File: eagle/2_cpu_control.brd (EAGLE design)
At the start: 160 x 100 mm, 50 parts, among them IC1 74154N, IC2 74LS139N, IC3 74LS138N, IC4 74LS139N, IC5 74LS00N, IC6 74LS32N, IC8 74LS08N

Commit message: All boards prepared for MMU extension
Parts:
- JP10: device pinhead:2X16 -> pinhead:2X18
- moved JP10 2.54 mm to (105.4, 6.99)
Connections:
- new net /FP: JP10.34
- new net /IO: JP10.35
- new net /NP_FAULT: JP10.36
- new net /WR_FAULT: JP10.33
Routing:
- net ALUOP1: track 84.2 -> 88.9 mm
- net ALUOP0: track 76.4 -> 80.0 mm
- net /LOAD_IR: track 106.6 -> 109.0 mm
- net /MEM2ALULO: track 146.8 -> 149.2 mm
- net /ALULO2MEM: track 143.8 -> 146.0 mm
- net /MEM2ALUHI: track 140.2 -> 141.8 mm
- net BUSCLKA: track 55.5 -> 53.9 mm, vias 2 -> 1
- net /ALUHI2MEM: track 141.2 -> 142.3 mm
- net +5V: track 479.5 -> 480.0 mm

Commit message: Removal of PPC started
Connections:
- removed net /LDPPC: JP10.11
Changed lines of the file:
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@@
 <contactref element="JP10" pad="30"/>
-</signal>
-<signal name="/LDPPC">
-<contactref element="JP10" pad="11"/>
 </signal>
 <signal name="BUSCLKA">

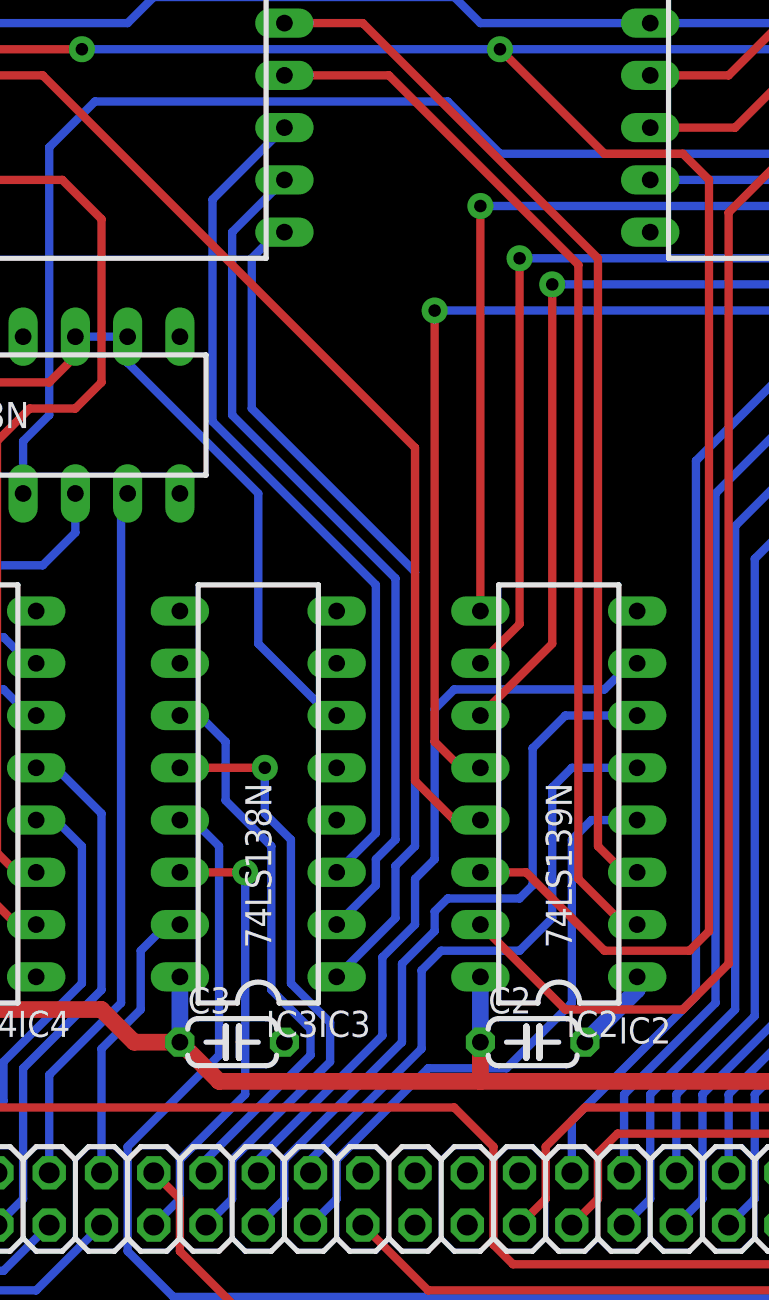
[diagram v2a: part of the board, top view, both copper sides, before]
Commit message: PPC removal completed, control card RBUS selector changed from LS138 to LS139, removed /LDPPC and /ENPPC signals
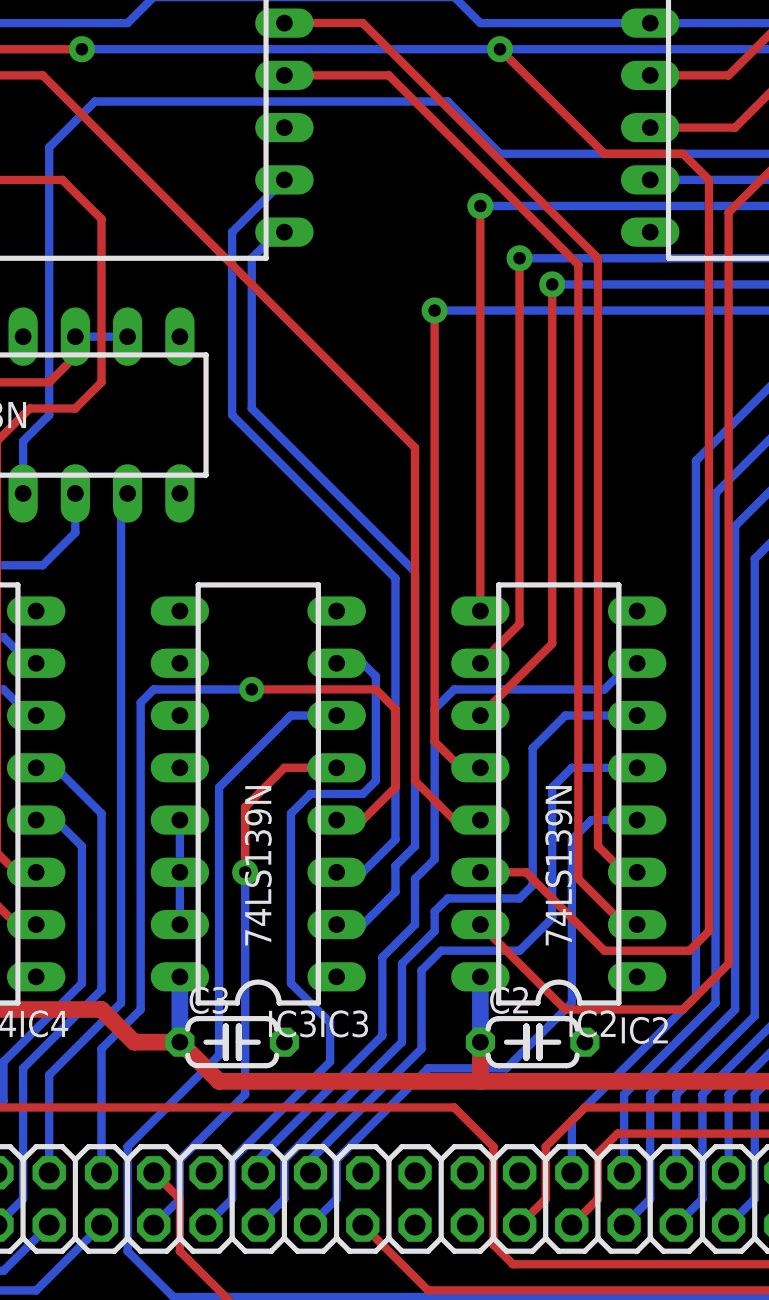
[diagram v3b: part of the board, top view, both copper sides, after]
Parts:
- IC3: value 74LS138N -> 74LS139N
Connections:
- removed net CRBUS2: IC3.3, UC1.19
- net +5V: no longer IC3.6
- net /ENABUS: now also IC3.6; no longer IC3.13
- net /ENIPTR: now also IC3.7; no longer IC3.12
- net /ENMSW: now also IC3.5; no longer IC3.14
- net /ENPPC: no longer IC3.11
- net /ENRMDR: now also IC3.4; no longer IC3.15
- net CRBUS0: now also IC3.2; no longer IC3.1
- net CRBUS1: now also IC3.3; no longer IC3.2
- net GND: now also IC3.1, IC3.13, IC3.14, IC3.15; no longer IC3.4, IC3.5
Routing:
- net CRBUS2: track 41.7 -> 0.00 mm
- net /ENRMDR: track 14.0 -> 44.0 mm, vias 0 -> 1
- net /ENPPC: track 27.5 -> 0.00 mm
- net +5V: track 480.0 -> 457.2 mm
- net /ENABUS: track 101.3 -> 108.8 mm
- net /ENMSW: track 22.2 -> 27.4 mm
- net /ENIPTR: track 30.2 -> 35.3 mm, vias 1 -> 0
- net CRBUS1: track 41.7 -> 39.9 mm
- net CRBUS0: track 41.9 -> 40.1 mm
- net GND: track 4.23 -> 5.08 mm
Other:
- board text removed: "74LS138N"

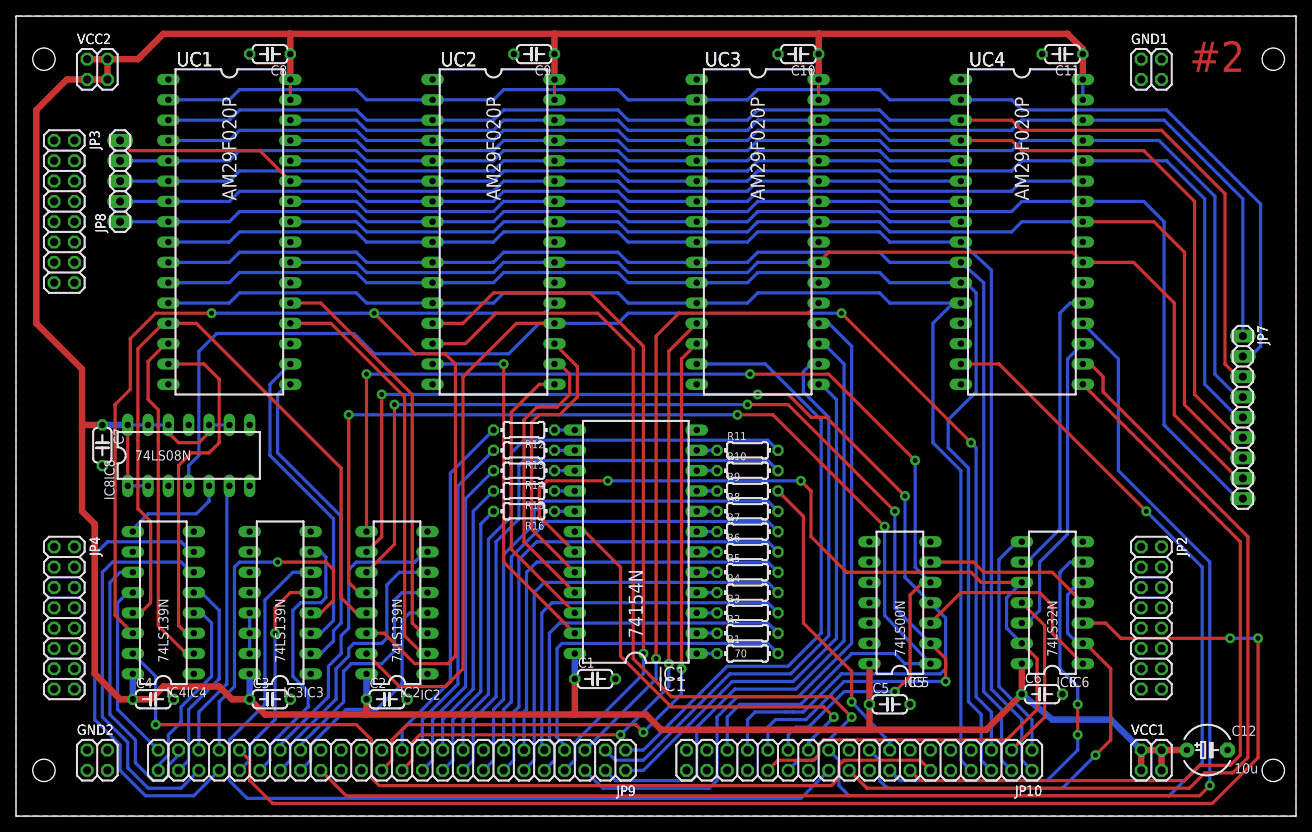
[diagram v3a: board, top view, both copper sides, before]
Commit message: Renumbered boards and schematic sheets
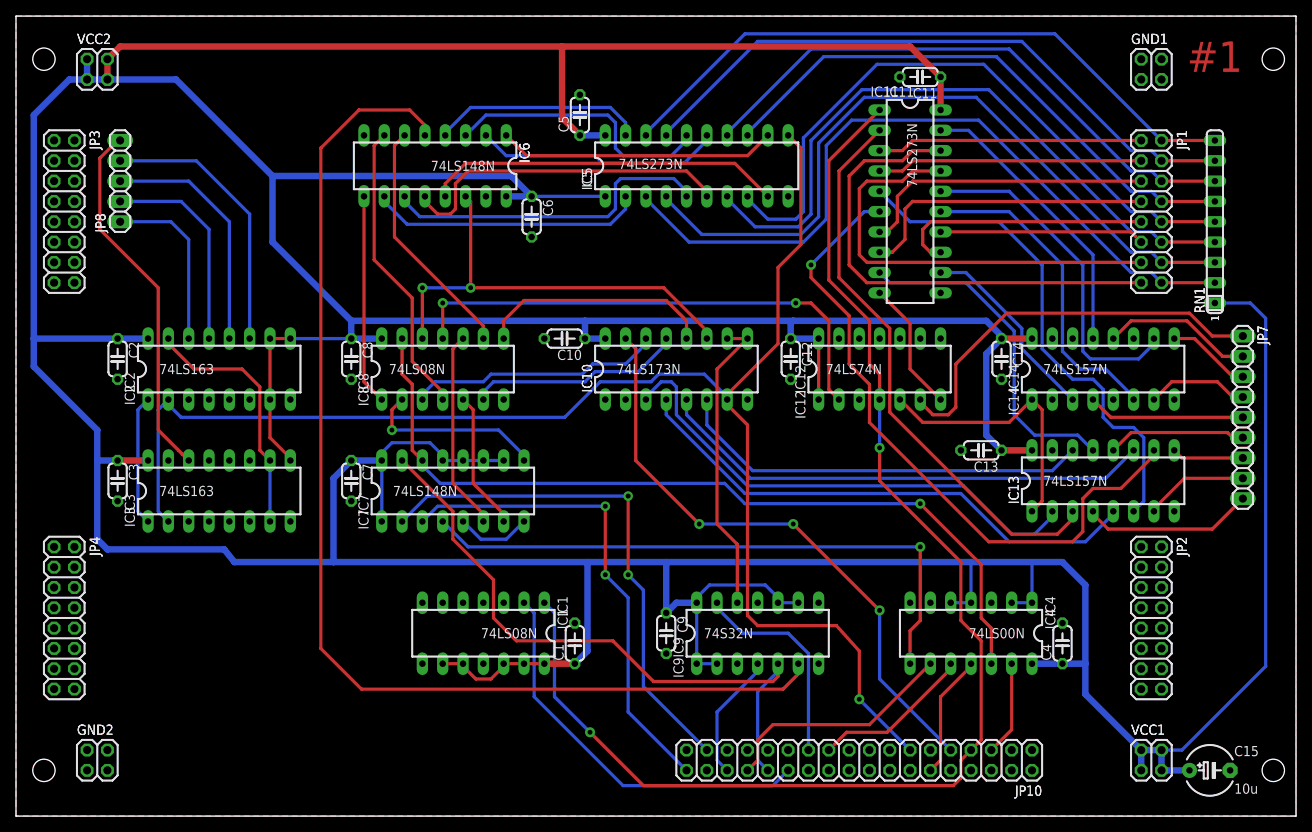
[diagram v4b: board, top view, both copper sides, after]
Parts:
- removed JP9: (no value), pinhead:2X24
- removed R1: 70, rcl:0204/7
- removed R10, R11, R12, R13, R14, R15, R16, R2, R3, R4, R5, R6, R7, R8, R9: (no value), rcl:0204/7
- removed UC1, UC2, UC3, UC4: AM29F020P, am29-memory:DIL32-6
- added C13, C14: 100n, rcl:C050-024X044
- added C15: 10u, rcl:E5-6
- added IC10: 74LS173N, 74xx-eu:DIL16
- added IC11: 74LS273N, 74xx-eu:DIL20
- added IC12: 74LS74N, 74xx-eu:DIL14
- added IC13, IC14: 74LS157N, 74xx-eu:DIL16
- added IC7: 74LS148N, 74xx-eu:DIL16
- added IC9: 74S32N, 74xx-eu:DIL14
- added JP1: (no value), pinhead:2X08
- added RN1: 4.7k, resistor-sil:SIL9
- C12: value 10u -> 100n; device rcl:E5-6 -> rcl:C050-024X044
- IC1: value 74154N -> 74LS08N; device 74xx-eu:DIL24-6 -> 74xx-eu:DIL14
- IC2, IC3: value 74LS139N -> 74LS163
- IC4: value 74LS139N -> 74LS00N; device 74xx-eu:DIL16 -> 74xx-eu:DIL14
- IC5: value 74LS00N -> 74LS273N; device 74xx-eu:DIL14 -> 74xx-eu:DIL20
- IC6: value 74LS32N -> 74LS148N; device 74xx-eu:DIL14 -> 74xx-eu:DIL16
- moved C4 113.9 mm to (130.8, 21.6), turned to 90 degrees
- moved IC4 101.0 mm to (119.4, 22.9), turned to 180 degrees
- moved IC6 94.5 mm to (52.4, 81.3), turned to 180 degrees
- moved C6 87.4 mm to (64.5, 74.9), turned to 270 degrees
- moved C5 83.2 mm to (70.5, 87.6), turned to 90 degrees
- moved C9 74.2 mm to (81.3, 22.9), turned to 270 degrees
- moved C12 71.4 mm to (96.8, 57.1), turned to 270 degrees
- moved IC5 60.2 mm to (85.1, 81.3), turned to 0 degrees
- moved C2 54.2 mm to (12.7, 57.1), turned to 270 degrees
- moved C10 46.0 mm to (68.6, 59.7)
- moved C8 39.4 mm to (41.9, 57.1), turned to 270 degrees
- moved IC2 36.7 mm to (25.4, 55.9), turned to 0 degrees
- moved IC8 33.5 mm to (53.3, 55.9)
- moved C3 33.3 mm to (12.7, 41.9), turned to 270 degrees
- moved C7 31.4 mm to (41.9, 41.9)
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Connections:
- removed net /ALUCARRYIN: JP9.2, UC3.17
- removed net /ALUSHR: JP9.1, UC3.15
- removed net /CARRY1: JP9.29
- removed net /CARRY3: JP9.31
- removed net /CNT_SP: IC6.12, UC4.19
- removed net /ENA: IC2.5, JP9.33
- removed net /ENALU: IC6.3, JP9.39
- removed net /ENDP: IC4.6, JP9.44
- removed net /ENIPTR: IC3.7, JP9.38
- removed net /ENLMDR: IC2.4, JP9.34
- removed net /ENMAR: IC4.4, JP9.48
- removed net /ENMSW: IC3.5, JP9.40
- removed net /ENPC: IC4.7, JP9.42
- removed net /ENPPC: JP9.37
- removed net /ENRMDR: IC3.4, JP9.41
- removed net /ENSP: IC4.5, JP9.46
- removed net /ENX: IC2.6, JP9.36
- removed net /ENY: IC2.7, JP9.35
- removed net /INC_MAR: JP9.32, UC4.20
- removed net /INC_PC: IC6.9, UC4.21
- removed net /LATCH_I: IC4.12, JP9.47
- removed net /LATCH_NONE: IC4.9, IC8.5
- removed net /LATCH_S: IC4.11, JP9.45
- removed net /LDA: JP9.14, R6.2
- removed net /LDAHI: JP9.11, R5.2
- removed net /LDALO: JP9.12, R4.2
- removed net /LDDP: JP9.22, R14.2
- removed net /LDMAR: JP9.23, R12.2
- removed net /LDMARHI: JP9.17, R11.2
- removed net /LDMARLO: JP9.18, R10.2
- removed net /LDMDR: JP9.9, R3.2
- removed net /LDMDRHI: JP9.10, R2.2
- removed net /LDMDRLO: JP9.7, R1.2
- removed net /LDMSW: JP9.20, R16.2
- removed net /LDPC: JP9.19, R15.2
- removed net /LDSP: JP9.21, R13.2
- removed net /LDX: JP9.13, R7.2
- removed net /LDY: JP9.16, R8.2
- removed net ADDRBUS0: IC4.2, UC1.14
- removed net ADDRBUS1: IC4.3, UC1.15
- removed net ALUMODE: JP9.3, UC3.18
- removed net ALUOP0: JP9.4, UC3.19
- removed net ALUOP1: JP9.6, UC3.20
- removed net ALUOP2: JP9.5, UC3.21
- removed net ALUOP3: JP9.8, UC2.13
- removed net ALURES0: JP9.25
- removed net ALURES8: JP9.27
- removed net BUSIFCMODE0: IC2.14, IC4.14, UC2.21
- removed net BUSIFCMODE1: IC2.13, IC4.13, UC1.13
- removed net CLBUS0: IC2.2, UC1.20
- removed net CLBUS1: IC2.3, UC1.21
- removed net CRBUS0: IC3.2, UC1.17
- removed net CRBUS1: IC3.3, UC1.18
- removed net LOAD0: IC1.23, UC2.15
- removed net LOAD1: IC1.22, UC2.17
- removed net LOAD2: IC1.21, UC2.18
- removed net LOAD3: IC1.20, UC2.19
- removed net LOAD_FLAGS0: JP9.24, UC3.13
- removed net LOAD_FLAGS1: JP9.26, UC3.14
- removed net MDRLDINHBT: IC8.6, JP9.43
- removed net N$31: IC1.1, R1.1
- removed net N$33: IC1.2, R2.1
- removed net N$34: IC1.3, R3.1
- removed net N$35: IC1.4, R4.1
- removed net N$36: IC1.5, R5.1
- removed net N$37: IC1.6, R6.1
- removed net N$38: IC1.7, R7.1
- removed net N$39: IC1.8, R8.1
- removed net N$40: IC1.9, R9.1
- removed net N$41: IC1.10, R10.1
- removed net N$42: IC1.11, R11.1
- removed net N$43: IC1.13, R12.1
- removed net N$44: IC1.14, R13.1
- removed net N$45: IC1.15, R14.1
- removed net N$56: IC1.17, R16.1
- new net /FAULT_PF: IC4.8, IC7.4
- new net /NEXTOP: IC1.6, IC10.10, IC10.9, IC9.12
- new net DBUS0: IC11.3, JP1.1
- new net DBUS1: IC11.4, JP1.3
- new net DBUS2: IC11.7, JP1.5
- new net DBUS3: IC11.8, JP1.7
- new net DBUS4: IC11.13, JP1.9
- new net DBUS5: IC11.14, JP1.11
- new net DBUS6: IC11.17, JP1.13
- new net DBUS7: IC11.18, JP1.15
- new net IRQ0: IC5.18, JP1.2, RN1.9
- new net IRQ1: IC5.17, JP1.4, RN1.8
- new net IRQ2: IC5.14, JP1.6, RN1.7
- new net IRQ3: IC5.13, JP1.8, RN1.6
- new net IRQ4: IC5.8, JP1.10, RN1.5
- new net IRQ5: IC5.7, JP1.12, RN1.4
- new net IRQ6: IC5.4, JP1.14, RN1.3
- new net IRQ7: IC5.3, JP1.16, RN1.2
- new net N$10: IC1.5, IC4.12, IC7.14, IC8.13
- new net N$11: IC10.14, IC8.3
- new net N$12: IC10.13, IC8.6
- new net N$13: IC10.12, IC8.8
- new net N$14: IC12.2, IC8.11
- new net N$16: IC11.5, IC13.6
- new net N$17: IC11.11, IC12.3, IC9.11
- new net N$18: IC10.3, IC13.2
- new net N$19: IC10.4, IC13.5
- new net N$2: IC2.15, IC3.10, IC3.7
- new net N$20: IC10.5, IC13.11
- new net N$21: IC10.6, IC13.14
- new net N$22: IC11.19, IC14.13
- new net N$23: IC11.16, IC14.10
- new net N$24: IC11.15, IC14.6
- new net N$25: IC11.12, IC14.3
- new net N$26: IC11.2, IC13.3
- new net N$27: IC6.5, IC9.6
- new net N$28: IC11.6, IC13.10
- new net N$3: IC7.9, IC8.2
- new net N$30: IC11.9, IC13.13
- new net N$4: IC6.7, IC8.4
- new net N$47: IC12.5, IC13.1, IC14.1
- new net N$5: IC7.7, IC8.5
- new net N$57: IC5.19, IC6.4
- new net N$58: IC5.16, IC6.3
- new net N$59: IC5.15, IC6.2
- new net N$6: IC7.6, IC8.10
- new net N$60: IC5.12, IC6.1
- new net N$61: IC5.9, IC6.13
- new net N$62: IC5.6, IC6.12
- new net N$63: IC5.5, IC6.11
- new net N$64: IC5.2, IC6.10
- new net N$7: IC6.6, IC8.9
- new net N$9: IC10.11, IC6.14, IC8.12
- net +5V: now also C12.1, C13.1, C14.1, C15.+, IC1.10, IC1.12, IC1.13, IC1.14, IC1.9, IC10.16, IC11.20, IC12.1, IC12.14, IC13.16, IC14.16, IC2.10, IC2.7, IC2.9, IC3.9, IC4.1, IC4.14, IC4.2, IC4.4, IC4.5, IC5.1, IC5.20, IC6.16, IC7.1, IC7.10, IC7.11, IC7.12, IC7.13, IC7.16, IC9.1, IC9.10, IC9.14, IC9.2, IC9.9, RN1.1; no longer C12.+, IC1.24, IC4.16, IC5.14, IC6.14, IC8.1, IC8.10, IC8.12, IC8.13, IC8.2, IC8.9, UC1.31, UC1.32, UC2.31, UC2.32, UC3.31, UC3.32, UC4.31, UC4.32
- net /ALUHI2MEM: no longer IC2.9, IC5.5
- net /ALULO2MEM: no longer IC2.10, IC5.4
- net /BUSIFCEN: now also IC4.13; no longer IC2.15, IC8.4, UC2.20
- net /CNTSP: no longer IC6.11
- net /ENABUS: no longer IC3.6
- net /ENMEM: no longer IC6.6
- net /FI: now also IC9.4
- net /FS: now also IC4.9
- net /INCPC: no longer IC6.8
- net /LATCHFLAGS: now also IC4.11; no longer IC4.15
- net /LDMEM: no longer R9.2
- net /LOAD_IR: now also IC1.2; no longer UC2.14
- net /MEM2ALUHI: no longer IC2.11, IC5.2
- net /MEM2ALULO: no longer IC2.12, IC5.1
- net /NP_FAULT: now also IC7.3
- net /RST: now also IC1.1, IC11.1, IC12.4
- net /WR_FAULT: now also IC7.2
- net BUSCLKA: now also IC9.13; no longer IC1.18
- net CLK0A: now also IC10.7, IC2.2, IC3.2, IC5.11
- net CLK0D: no longer IC6.2, IC6.5
- net CNT0: now also IC2.14; no longer UC1.8, UC2.8, UC3.8, UC4.8
- net CNT1: now also IC2.13; no longer UC1.7, UC2.7, UC3.7, UC4.7
- net CNT2: now also IC2.12; no longer UC1.6, UC2.6, UC3.6, UC4.6
- net CNT3: now also IC2.11; no longer UC1.5, UC2.5, UC3.5, UC4.5
- net CNT4: now also IC3.14; no longer UC1.27, UC2.27, UC3.27, UC4.27
- net FAULT: now also IC7.15, IC9.5; no longer IC1.19, IC6.10, IC6.13
- net FC: no longer UC1.9, UC2.9, UC3.9, UC4.9
- net FN: no longer UC1.11, UC2.11, UC3.11, UC4.11
- net FV: no longer UC1.12, UC2.12, UC3.12, UC4.12
- net FZ: no longer UC1.10, UC2.10, UC3.10, UC4.10
- net GND: now also C12.2, C13.2, C14.2, C15.-, IC1.7, IC10.1, IC10.2, IC10.8, IC11.10, IC12.10, IC12.11, IC12.12, IC12.13, IC12.7, IC13.15, IC13.8, IC14.11, IC14.14, IC14.15, IC14.2, IC14.5, IC14.8, IC2.3, IC2.4, IC2.5, IC2.6, IC3.3, IC3.4, IC3.5, IC3.6, IC4.7, IC6.8, IC7.5, IC7.8, IC9.7; no longer C12.-, IC1.12, IC2.1, IC3.1, IC3.13, IC3.14, IC3.15, IC4.1, IC4.8, IC5.12, IC5.13, IC5.7, IC5.9, IC6.7, UC1.16, UC1.22, UC1.24, UC2.16, UC2.22, UC2.24, UC3.16, UC3.22, UC3.24, UC4.16, UC4.22, UC4.24
- net MEMSEG: no longer UC4.17
- net N$1: now also IC6.9, IC8.1; no longer IC1.16, R15.1
- net N$15: now also IC1.3, IC1.4; no longer IC5.6, IC6.4
- net N$8: now also IC2.1, IC3.1; no longer IC5.3, IC6.1
- net OP0: now also IC13.4; no longer UC1.26, UC2.26, UC3.26, UC4.26
- net OP1: now also IC13.7; no longer UC1.23, UC2.23, UC3.23, UC4.23
- net OP2: now also IC13.9; no longer UC1.25, UC2.25, UC3.25, UC4.25
- net OP3: now also IC13.12; no longer UC1.4, UC2.4, UC3.4, UC4.4
- net OP4: now also IC14.4; no longer UC1.28, UC2.28, UC3.28, UC4.28
- net OP5: now also IC14.7; no longer UC1.29, UC2.29, UC3.29, UC4.29
- net OP6: now also IC14.9; no longer UC1.3, UC2.3, UC3.3, UC4.3
- net OP7: now also IC14.12; no longer UC1.2, UC2.2, UC3.2, UC4.2
- net OP8: now also IC12.6; no longer UC1.30, UC2.30, UC3.30, UC4.30
- net PROT: now also IC4.10; no longer UC4.15
- net RST: now also IC10.15
- net SP_DIR: no longer UC4.18
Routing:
- net +5V: track 457.2 -> 830.2 mm
- net /BUSIFCEN: track 229.5 -> 11.8 mm, vias 2 -> 0
- net CLK0A: track 0.00 -> 187.6 mm, vias 0 -> 1
- net /INC_MAR: track 177.3 -> 0.00 mm, vias 1 -> 0
- net FC: track 172.0 -> 0.00 mm
- net /ENALU: track 171.6 -> 0.00 mm, vias 2 -> 0
- net FZ: track 168.4 -> 0.00 mm
- net FN: track 168.0 -> 0.00 mm
- net FV: track 164.6 -> 0.00 mm
- net /RST: track 0.00 -> 163.1 mm, vias 0 -> 2
- net BUSIFCMODE0: track 155.8 -> 0.00 mm, vias 2 -> 0
- net OP6: track 163.2 -> 10.5 mm
- net OP3: track 167.0 -> 17.4 mm
- net /MEM2ALULO: track 149.2 -> 0.00 mm, vias 3 -> 0
- net OP7: track 165.6 -> 19.0 mm
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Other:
- board text added: "#1"
- board text added: "1"
- board text added: "74LS148N"
- board text added: "74LS157N"
- board text added: "74LS163"
- board text added: "74LS173N"
- board text added: "74LS273N"
- board text added: "74LS74N"
- board text added: "74S32N"
- board text added: "IC10"
- board text added: "IC11"
- board text added: "IC12"
- board text added: "IC13"
- board text added: "IC14"
- board text added: "IC7"
- board text added: "IC9"
- board text added: "JP1"
- board text added: "RN1"
- board text removed: "#2"
- board text removed: "70"
- board text removed: "74154N"
- board text removed: "74LS139N"
- board text removed: "74LS32N"
- board text removed: "AM29F020P"
- board text removed: "JP9"
- board text removed: "UC1"
- board text removed: "UC2"
- board text removed: "UC3"
- board text removed: "UC4"

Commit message: Sat Feb  6 20:10:54 CET 2016
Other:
- board text added: "#2"
- board text removed: "#1"
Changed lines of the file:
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@@
 <circle x="157.1625" y="5.715" radius="2.286" width="0" layer="42"/>
 <circle x="3.4925" y="5.715" radius="2.286" width="0" layer="42"/>
-<text x="146.3675" y="93.0275" size="3.81" layer="1" font="vector" ratio="15">#1</text>
+<text x="146.3675" y="93.0275" size="3.81" layer="1" font="vector" ratio="15">#2</text>
 <wire x1="68.707" y1="19.939" x2="69.215" y2="19.431" width="0.254" layer="121" curve="90"/>
 <wire x1="70.485" y1="19.431" x2="70.993" y2="19.939" width="0.254" layer="121" curve="90"/>

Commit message: Mon Feb  8 16:27:58 CET 2016
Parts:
- added IC15, IC16: 74LS163, 74xx-eu:DIL16
- JP8: device pinhead:1X05 -> pinhead:1X06
- moved JP8 1.27 mm to (13.0, 78.1)
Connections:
- removed net N$15: IC1.3, IC1.4
- new net /FRET: IC2.9, IC3.9, JP8.1
- new net /MEMOP: JP10.11
- new net N$29: IC15.12, IC3.5
- new net N$31: IC16.12, IC2.5
- new net N$32: IC16.14, IC2.3
- new net N$33: IC16.13, IC2.4
- new net N$34: IC16.11, IC2.6
- new net N$35: IC15.14, IC3.3
- new net N$36: IC15.13, IC3.4
- new net N$37: IC15.11, IC3.6
- new net VCC: IC15.16, IC16.16
- net +5V: now also IC15.1, IC16.1; no longer IC2.9, IC3.9
- net /NEXTOP: now also IC2.1, IC3.1
- net CLK0A: now also IC15.2, IC16.2
- net CNT0: now also IC16.3, JP8.2; no longer JP8.1
- net CNT1: now also IC16.4, JP8.3; no longer JP8.2
- net CNT2: now also IC16.5, JP8.4; no longer JP8.3
- net CNT3: now also IC16.6, JP8.5; no longer JP8.4
- net CNT4: now also IC15.3, JP8.6; no longer JP8.5
- net GND: now also IC15.10, IC15.7, IC15.8, IC16.10, IC16.7, IC16.8; no longer IC2.3, IC2.4, IC2.5, IC2.6, IC3.3, IC3.4, IC3.5, IC3.6
- net N$10: now also IC1.4, IC15.9, IC16.9; no longer IC1.5
- net N$8: now also IC1.3, IC1.5; no longer IC2.1, IC3.1
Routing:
- net N$8: track 16.3 -> 0.00 mm
- net /NEXTOP: track 38.2 -> 54.5 mm
- net +5V: track 830.2 -> 819.7 mm
- net IRQ4: track 81.4 -> 74.7 mm

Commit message: 2016-02-09 13:30
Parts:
- added C16, C17, C18: 100n, rcl:C050-024X044
- added IC17: 74LS04N, 74xx-eu:DIL14
- moved C1 2.22 mm to (69.8, 23.8)
- moved IC1 2.22 mm to (58.4, 25.1)
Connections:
- removed net VCC: IC15.16, IC16.16
- new net N$15: IC17.2, IC9.10
- new net N$38: IC2.1, IC3.1, IC9.8
- net +5V: now also C16.1, C17.1, C18.1, IC15.16, IC16.16, IC17.14; no longer IC9.10, IC9.9
- net /FRET: now also IC17.1
- net /NEXTOP: now also IC9.9; no longer IC2.1, IC3.1
- net GND: now also C16.2, C17.2, C18.2, IC17.11, IC17.13, IC17.3, IC17.5, IC17.7, IC17.9
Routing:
- net +5V: track 819.7 -> 878.6 mm
- net N$38: track 0.00 -> 16.3 mm
- net /NEXTOP: track 54.5 -> 38.2 mm
- net N$27: track 143.5 -> 135.6 mm
- net IRQ4: track 74.7 -> 81.4 mm
- net FAULT: track 80.0 -> 80.8 mm
- net /LOAD_IR: track 49.4 -> 50.2 mm
- net /RST: track 163.1 -> 163.9 mm

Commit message: 2016-02-09 18:12
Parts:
- moved C9 1.27 mm to (81.3, 24.1)
- moved C1 0.64 mm to (69.8, 24.4)
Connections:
- net GND: now also IC15.4, IC15.5, IC15.6
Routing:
- net N$38: track 16.3 -> 144.5 mm
- net /FRET: track 0.00 -> 94.5 mm
- net N$15: track 0.00 -> 69.3 mm
- net CLK0A: track 187.6 -> 249.5 mm
- net N$10: track 104.8 -> 163.9 mm, vias 1 -> 2
- net /NEXTOP: track 38.2 -> 93.5 mm
- net CNT4: track 45.8 -> 99.2 mm
- net N$17: track 0.00 -> 51.6 mm, vias 0 -> 1
- net CNT1: track 26.2 -> 65.7 mm
- net CNT3: track 34.5 -> 74.0 mm
- net CNT2: track 30.4 -> 69.8 mm
- net CNT0: track 21.9 -> 61.3 mm
- net N$34: track 0.00 -> 24.2 mm
- net N$33: track 0.00 -> 24.2 mm
- net N$32: track 0.00 -> 24.2 mm
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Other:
- board text added: "C1"
- board text added: "C10"
- board text added: "C11"
- board text added: "C12"
- board text added: "C13"
- board text added: "C14"
- board text added: "C16"
- board text added: "C17"
- board text added: "C18"
- board text added: "C3"
- board text added: "C5"
- board text added: "C6"
- board text added: "C7"
- board text added: "C8"
- board text added: "C9"
- board text added: "IC15"
- board text added: "IC16"
- board text added: "IC17"
- board text removed: "10u"
- board text removed: "74LS00N"
- board text removed: "74LS08N"
- board text removed: "74LS148N"
- board text removed: "74LS157N"
- board text removed: "74LS163"
- board text removed: "74LS173N"
- board text removed: "74LS273N"
- board text removed: "74LS74N"
- board text removed: "74S32N"
